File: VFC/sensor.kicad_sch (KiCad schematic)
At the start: 33 parts, among them U2 BMP388, U5 ESP32-C3, U6 ICM-42688-P, U7 W25N04KVZEIR, Y2 C3E-40.000-10-1015-X-R

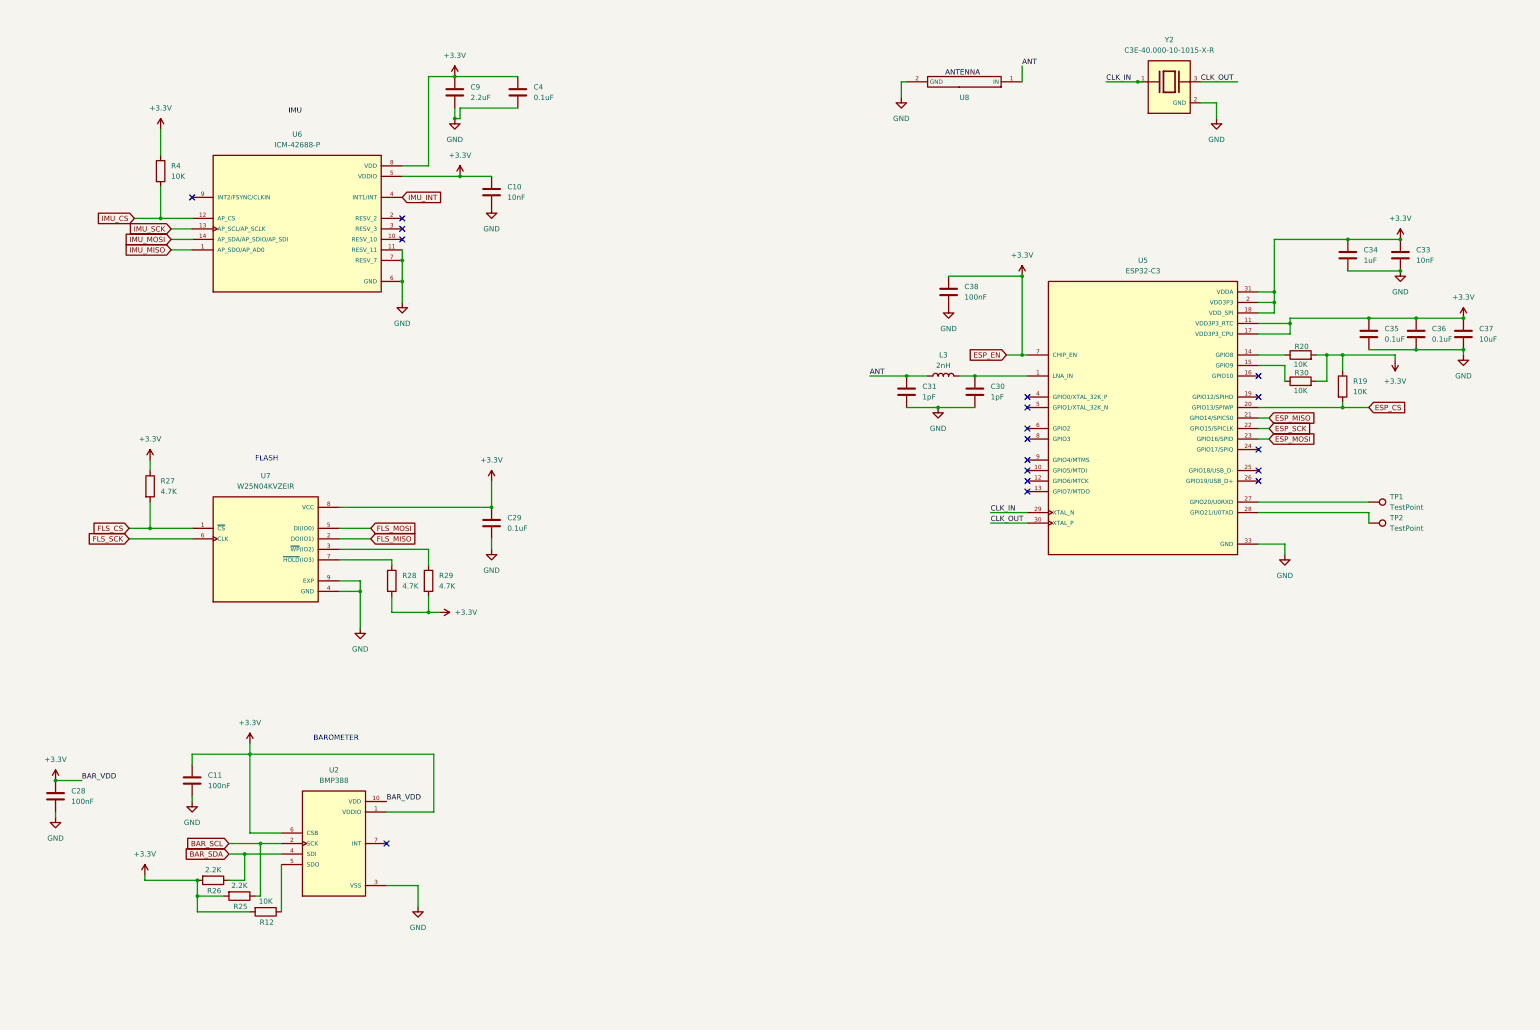
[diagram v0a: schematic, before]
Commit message: VFC PCB components placements complete
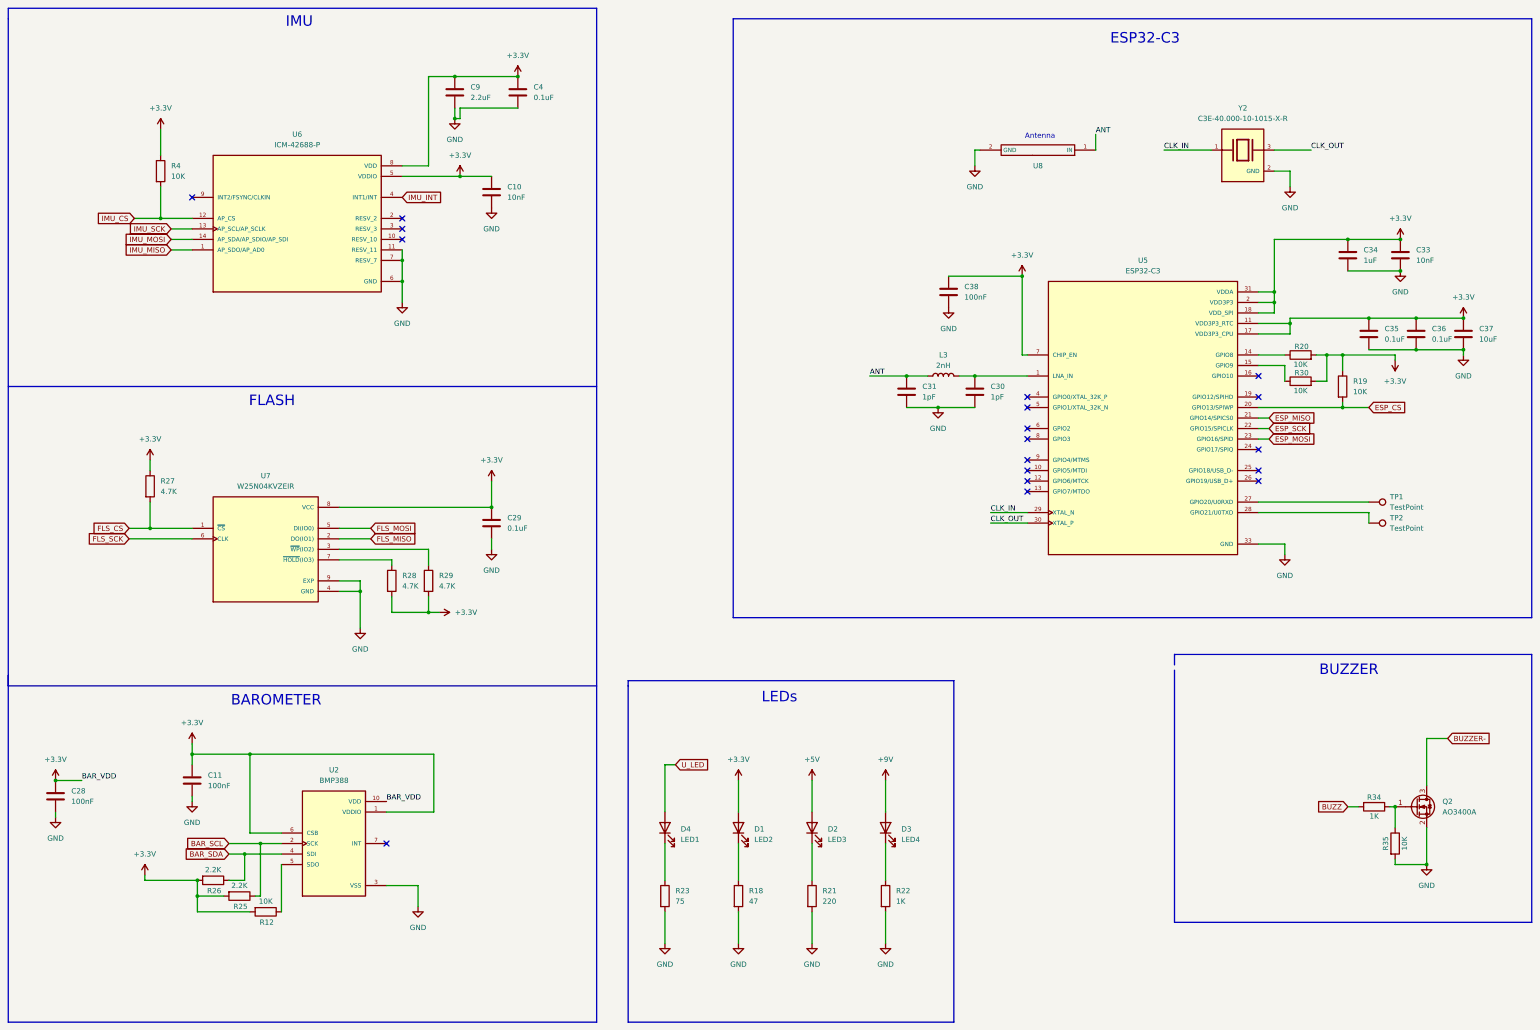
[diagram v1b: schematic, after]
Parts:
- added D1: LED2, LED_SMD:LED_0805_2012Metric, symbol Device:LED
- added D2: LED3, LED_SMD:LED_0805_2012Metric, symbol Device:LED
- added D3: LED4, LED_SMD:LED_0805_2012Metric, symbol Device:LED
- added D4: LED1, LED_SMD:LED_0805_2012Metric, symbol Device:LED
- added Q2: AO3400A, Package_TO_SOT_SMD:SOT-23, symbol Transistor_FET:AO3400A
- added R18: 47, Resistor_SMD:R_0402_1005Metric, symbol Device:R
- added R21: 220, Resistor_SMD:R_0402_1005Metric, symbol Device:R
- added R22, R34: 1K, Resistor_SMD:R_0402_1005Metric, symbol Device:R
- added R23: 75, Resistor_SMD:R_0402_1005Metric, symbol Device:R
- added R35: 10K, Resistor_SMD:R_0402_1005Metric, symbol Device:R
- C37: footprint Capacitor_SMD:C_0402_1005Metric -> Capacitor_SMD:C_0603_1608Metric
- L3: footprint (none) -> Inductor_SMD:L_0402_1005Metric
- R12, R19, R20, R25, R26, R27, R28, R29, R30, R4: footprint (none) -> Resistor_SMD:R_0402_1005Metric
- TP1, TP2: footprint (none) -> TestPoint:TestPoint_Pad_D1.0mm
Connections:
- net +3.3V: now also D1.2 (A)
- net GND: now also Q2.2 (S), R18.2, R21.2, R22.2, R23.2, R35.2
- new net: D2.1 (K), R21.1
- new net: Q2.1 (G), R34.1, R35.1
- new net: D4.1 (K), R23.1
- new net: D1.1 (K), R18.1
- new net: D3.1 (K), R22.1
- new net +5V: D2.2 (A)
- new net +9V: D3.2 (A)
- new net BUZZ: R34.2
- new net BUZZER-: Q2.3 (D)
- new net U_LED: D4.2 (A)
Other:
- note added: "Antenna"
- note added: "BUZZER"
- note added: "ESP32-C3"
- note added: "LEDs"
- moved on the sheet: U8, Y2

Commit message: VFC PCB traces update
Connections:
- net +3.3V: no longer C10.1, C11.1, C28.1, C4.1, C9.1, R12.2, R25.2, R26.2, R4.1, U2.1 (VDDIO), U2.10 (VDD), U2.6 (CSB), U6.5 (VDDIO), U6.8 (VDD)
- new net +3.3VA: C10.1, C11.1, C28.1, C4.1, C9.1, R12.2, R25.2, R26.2, R4.1, U2.1 (VDDIO), U2.10 (VDD), U2.6 (CSB), U6.5 (VDDIO), U6.8 (VDD)
